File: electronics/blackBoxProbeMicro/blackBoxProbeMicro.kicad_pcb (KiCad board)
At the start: 4 copper layers, 29 x 29 mm, 67 parts, among them J1 USB-C, J2 JTAG_2X05, J3 JTAG_2X05, J4 DevBoardUartOutput, Q1 BSD840N, Q2 NTJD4152P, U1 MCP1702-MB, U2 DT1446-04S, U3 STM32F103CBT, Y1 8MHz

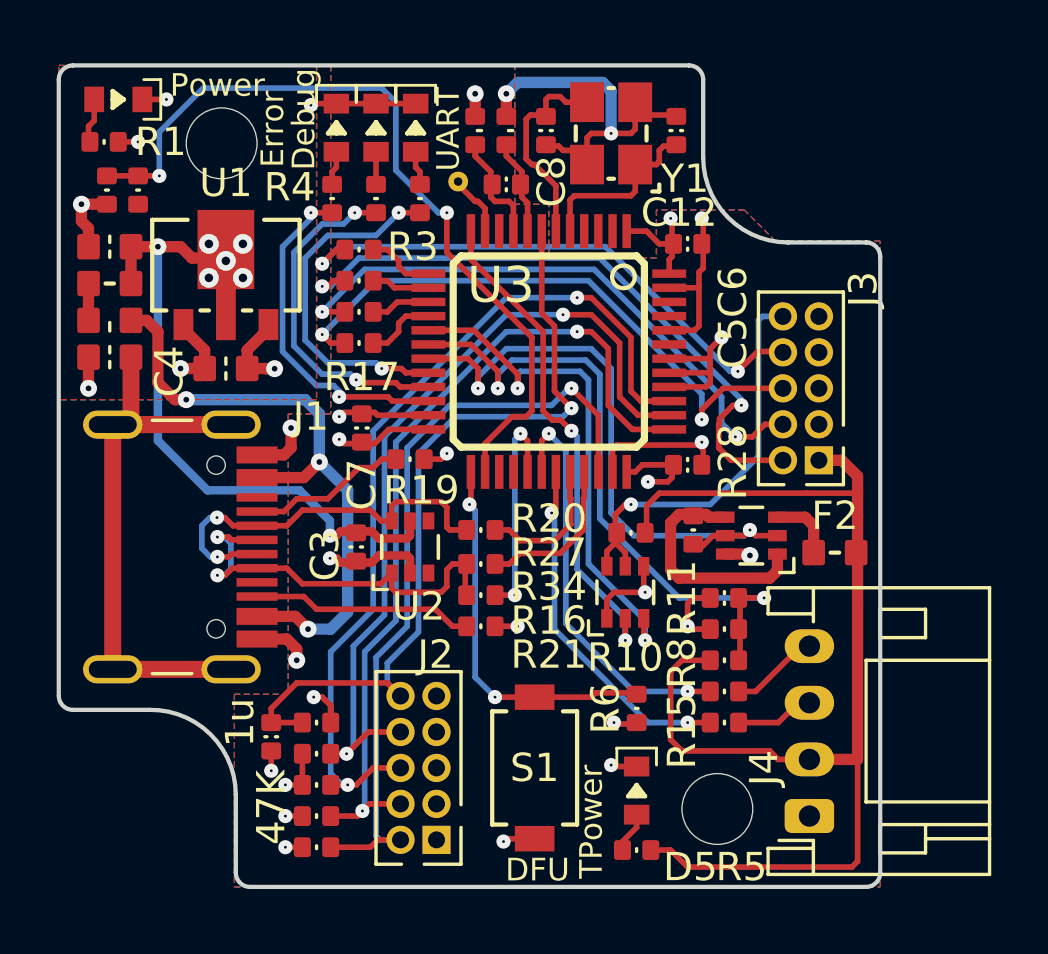
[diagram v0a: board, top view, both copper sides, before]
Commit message: some trace optimizations
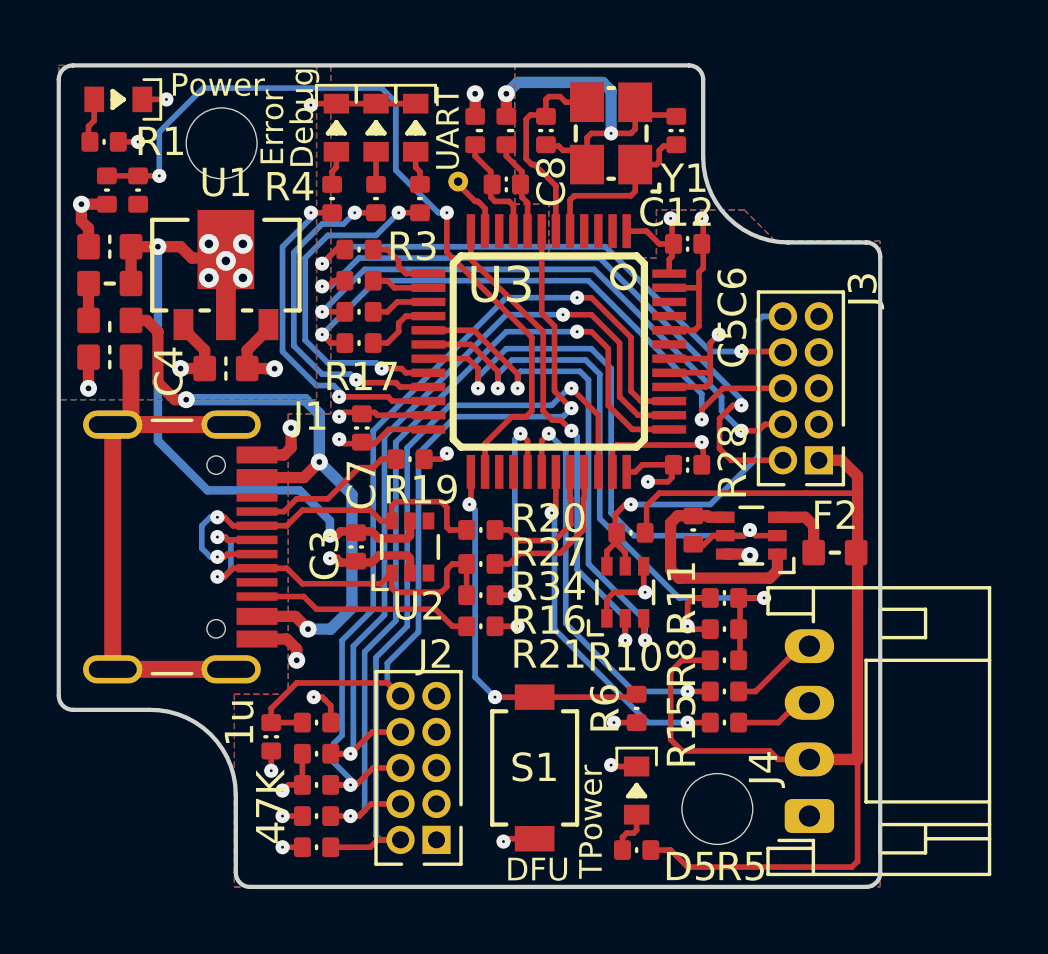
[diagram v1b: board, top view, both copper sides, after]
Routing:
- net /PROBE_E_TDI: track 19.6 -> 19.0 mm
- net /MCU_TCK: track 30.3 -> 30.8 mm

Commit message: WIP updating parts and PCB, replacing silk parts
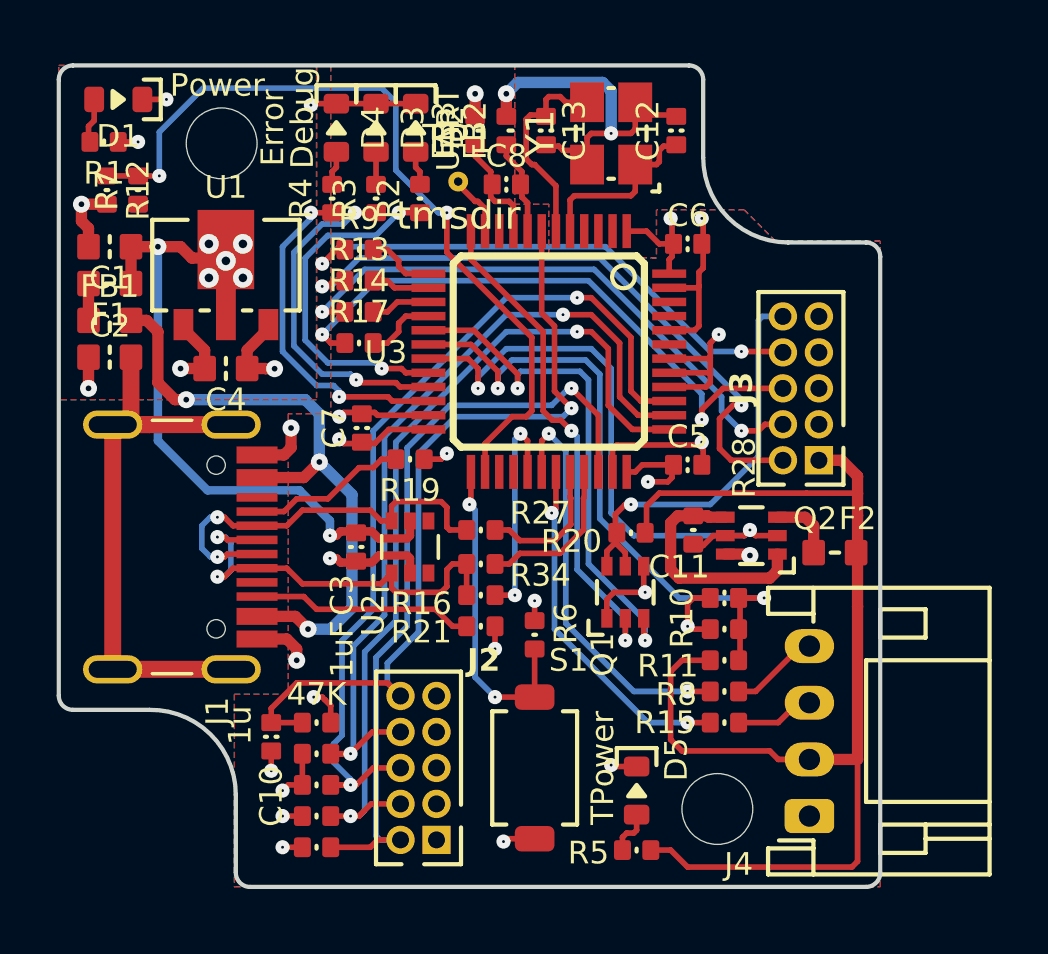
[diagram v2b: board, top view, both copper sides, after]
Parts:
- C1, C2, C4: footprint SquantorRcl:C_0603 -> SquantorCapacitor:C_0603
- C10, C11, C12, C13, C3, C5, C6, C7, C8: footprint SquantorRcl:C_0402 -> SquantorCapacitor:C_0402
- F1, F2: footprint SquantorRcl:F_0603_hand -> SquantorFuse:F_0603_hand
- FB1: footprint SquantorRcl:L_0603 -> SquantorInductor:L_0603
- FB2, FB3: footprint SquantorRcl:L_0402 -> SquantorInductor:L_0402
- J4: footprint Connector_JST:JST_PH_S4B-PH-K_1x04_P2.00mm_Horizontal -> SquantorConnectors:JST_PH_S4B-PH-K_1x04_P2.00mm_Horizontal
- R1, R10, R11, R12, R13, R14, R15, R16, R17, R18, R19, R2, R20, R21, R22, R23, R24, R25, R27, R28, R3, R34, R4, R5, R6, R7, R8, R9: footprint SquantorRcl:R_0402_hand -> SquantorResistor:R_0402_hand
- moved R6 4.44 mm to (149.8, 107.1), turned to -90 degrees
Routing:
- net /BUTTON: track 13.4 -> 11.4 mm

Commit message: WIP relayout on new DRC rules
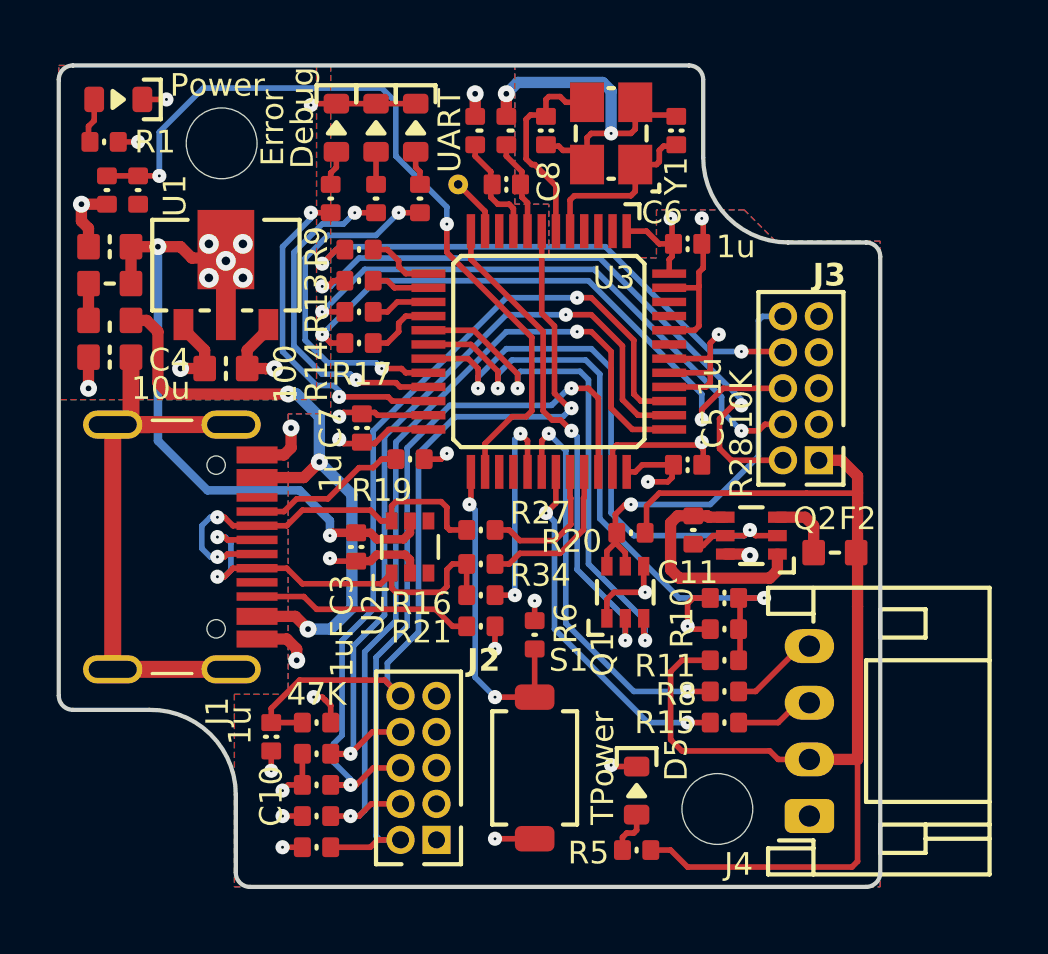
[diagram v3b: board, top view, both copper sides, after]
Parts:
- C2: value 100N -> 100n
- moved TP1 0.10 mm to (147.1, 91.2)
- moved R4 0.05 mm to (142.6, 91.7)

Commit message: adjustments of silk, fixing ERC errors
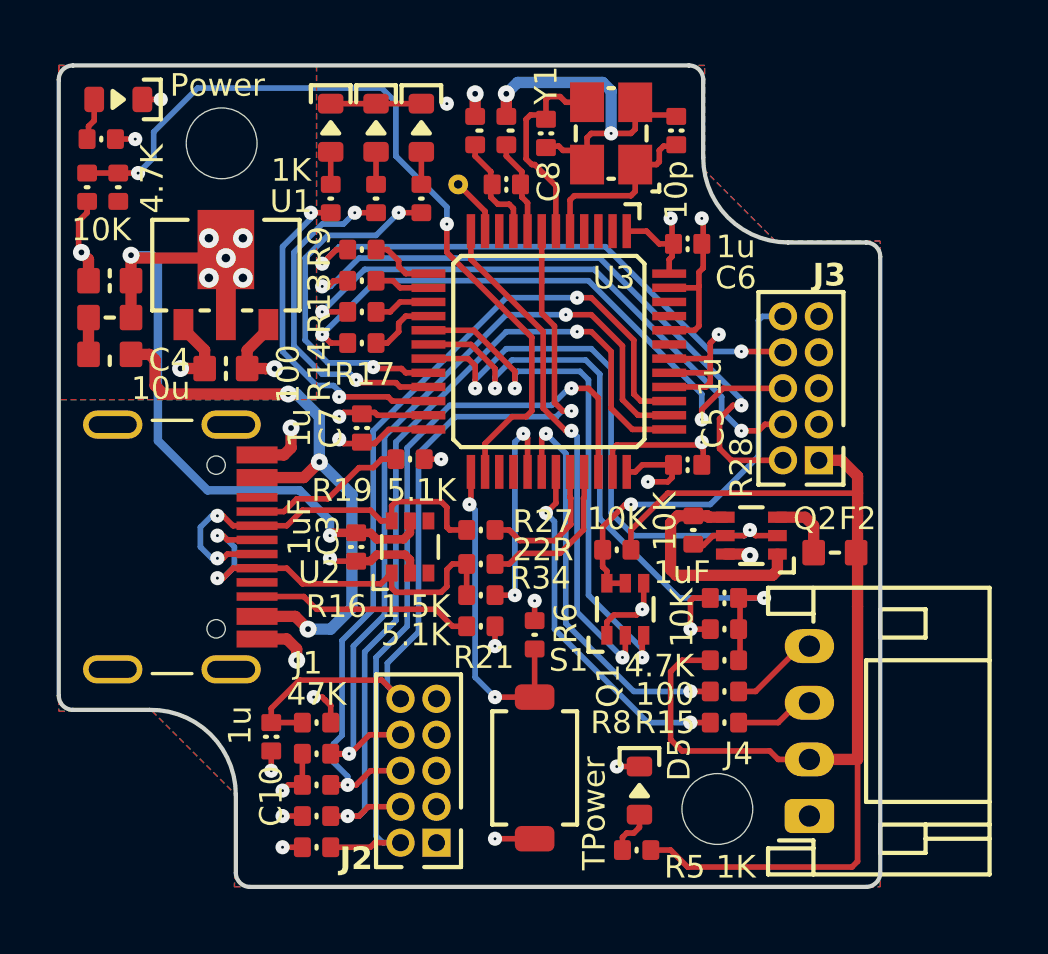
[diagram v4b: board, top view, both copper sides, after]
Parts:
- removed C2: 100n, SquantorCapacitor:C_0603
- N2: value V:20231214 -> V:20240121
- R27, R34: value 22 -> 22R
- moved F1 1.20 mm to (134.8, 95.9)
- moved FB1 1.20 mm to (134.8, 97.2)
- moved C1 1.20 mm to (134.8, 94.6)
- moved R20 0.78 mm to (152.7, 104.1)
- moved R7 0.71 mm to (135.1, 91.3)
- moved R12 0.71 mm to (134.0, 91.3)
- moved Q1 0.60 mm to (153.0, 106.2)
- moved D2 0.20 mm to (145.8, 89.2)
- moved D4 0.20 mm to (142.6, 89.2)
- moved R1 0.14 mm to (134.5, 89.6)
- moved C13 0.10 mm to (150.2, 89.4)
- moved J2 0.10 mm to (145.7, 111.9)
- moved D5 0.10 mm to (153.5, 112.6)
- moved R13 0.10 mm to (143.7, 94.6)
- moved R14 0.10 mm to (143.7, 95.7)
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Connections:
- J1 pad S: Net-(J1-Shield) -> /VSS
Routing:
- net Net-(J1-Shield): track 20.0 -> 0.00 mm
- net /VSS: track 55.8 -> 53.7 mm, vias 21 -> 20
- net /VUSB: track 23.9 -> 25.2 mm
- net /VBUS: track 21.2 -> 20.2 mm
- net /PROBE_VDD: track 41.9 -> 42.8 mm
- net /PROBE_I_RST: track 17.5 -> 18.2 mm
- net /PROBE_I_RST_SEN: track 18.3 -> 18.9 mm
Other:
- board text removed: "Debug"
- board text removed: "Error"
- board text removed: "UART"

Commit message: all planes are now VSS planes, some routing improvements
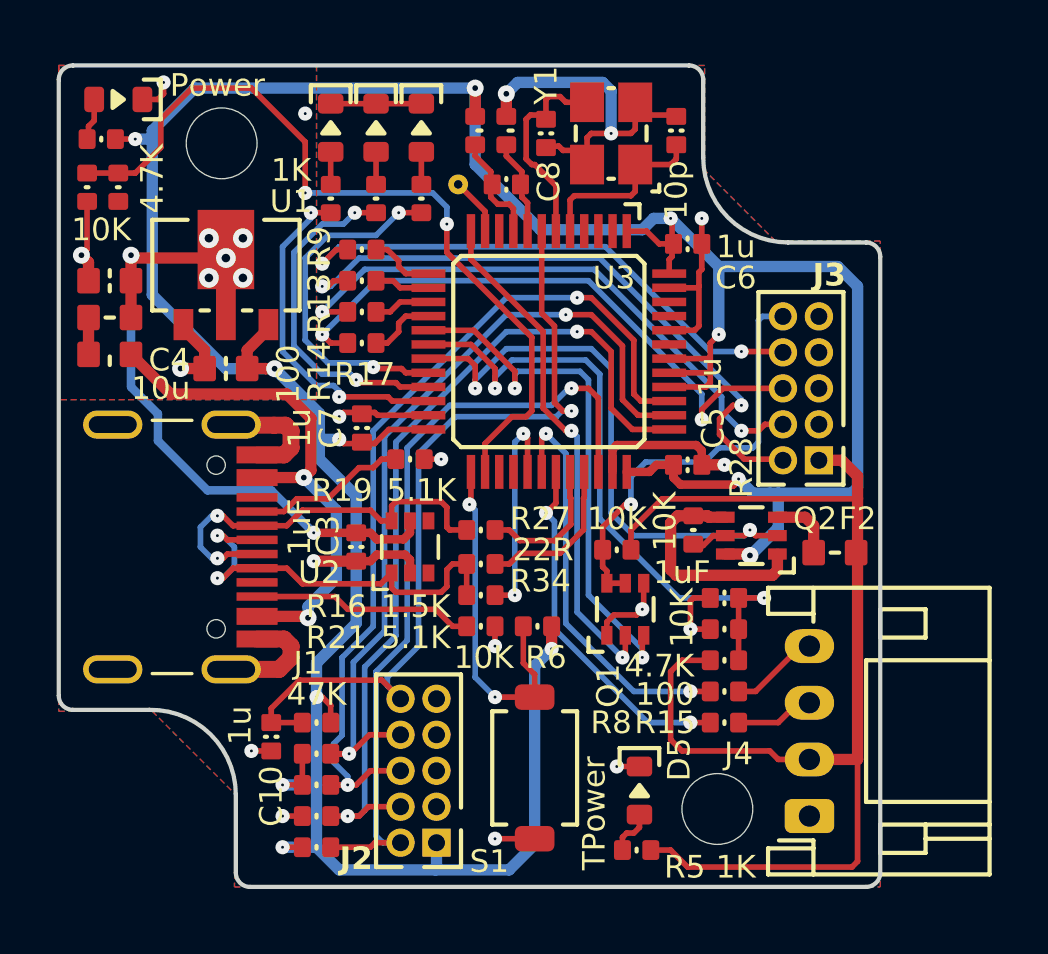
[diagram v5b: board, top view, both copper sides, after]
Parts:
- N2: value V:20240121 -> V:20240202
- moved R6 0.32 mm to (149.9, 106.8), turned to 180 degrees
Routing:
- net /VDD: track 26.3 -> 125.3 mm
- net /VSS: track 53.7 -> 60.3 mm, vias 20 -> 18
- net /VBUS: track 20.2 -> 17.4 mm, vias 3 -> 2
- net /BUTTON: track 11.4 -> 12.4 mm
- net /VUSB: track 25.2 -> 24.3 mm
- added copper zone on In2.Cu, net /VSS
- removed copper zone on In2.Cu, net /VDD

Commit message: reviewed and ready for production
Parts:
- N2: value V:20240202 -> V:20240216
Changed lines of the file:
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@@
         (effects (font (size 1 1) (thickness 0.15)) (justify mirror))
     )
-    (fp_text value "V:20240202" (at 0.8 0.1) (layer "B.SilkS")
+    (fp_text value "V:20240216" (at 0.8 0.1) (layer "B.SilkS")
         (effects (font (size 0.8 0.8) (thickness 0.15)) (justify mirror))
     )

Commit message: prepared for production
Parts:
- N2: value V:20240216 -> V:20240218
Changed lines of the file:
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@@
         (effects (font (size 1 1) (thickness 0.15)) (justify mirror))
     )
-    (fp_text value "V:20240216" (at 0.8 0.1) (layer "B.SilkS")
+    (fp_text value "V:20240218" (at 0.8 0.1) (layer "B.SilkS")
         (effects (font (size 0.8 0.8) (thickness 0.15)) (justify mirror))
     )
@@
   (segment (start 154.6 103.15) (end 154.6 104.8) (width 0.4) (layer "F.Cu") (net 53))
   (segment (start 156.53 102.95) (end 155.95 102.95) (width 0.4) (layer "F.Cu") (net 53))
+  (segment (start 136.3 98.6) (end 135.55 97.85) (width 0.4) (layer "F.Cu") (net 61))
+  (segment (start 141.75 106.45) (end 140.7 106.45) (width 0.4) (layer "F.Cu") (net 61))
+  (segment (start 141.65 101.55) (end 141.9 101.3) (width 0.4) (layer "F.Cu") (net 61))
+  (segment (start 141.8 106.5) (end 141.75 106.45) (width 0.4) (layer "F.Cu") (net 61))
+  (segment (start 141.044975 98.6) (end 136.3 98.6) (width 0.4) (layer "F.Cu") (net 61))
+  (segment (start 135.55 97.85) (end 135.55 97.2) (width 0.4) (layer "F.Cu") (net 61))
   (segment (start 141.9 101.3) (end 141.9 99.455025) (width 0.4) (layer "F.Cu") (net 61))
-  (segment (start 141.75 106.45) (end 140.7 106.45) (width 0.4) (layer "F.Cu") (net 61))
-  (segment (start 141.044975 98.6) (end 136.95 98.6) (width 0.4) (layer "F.Cu") (net 61))
-  (segment (start 136.95 98.6) (end 135.55 97.2) (width 0.4) (layer "F.Cu") (net 61))
-  (segment (start 141.8 106.5) (end 141.75 106.45) (width 0.4) (layer "F.Cu") (net 61))
   (segment (start 141.9 99.455025) (end 141.044975 98.6) (width 0.4) (layer "F.Cu") (net 61))
-  (segment (start 141.65 101.55) (end 141.9 101.3) (width 0.4) (layer "F.Cu") (net 61))
   (segment (start 141.65 101.55) (end 140.7 101.55) (width 0.4) (layer "F.Cu") (net 61))
   (via (at 141.65 101.55) (size 0.6) (drill 0.2) (layers "F.Cu" "B.Cu") (net 61))
